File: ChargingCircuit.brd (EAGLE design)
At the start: 100 x 80 mm, 22 parts, among them U1 MAX745EACSSOP

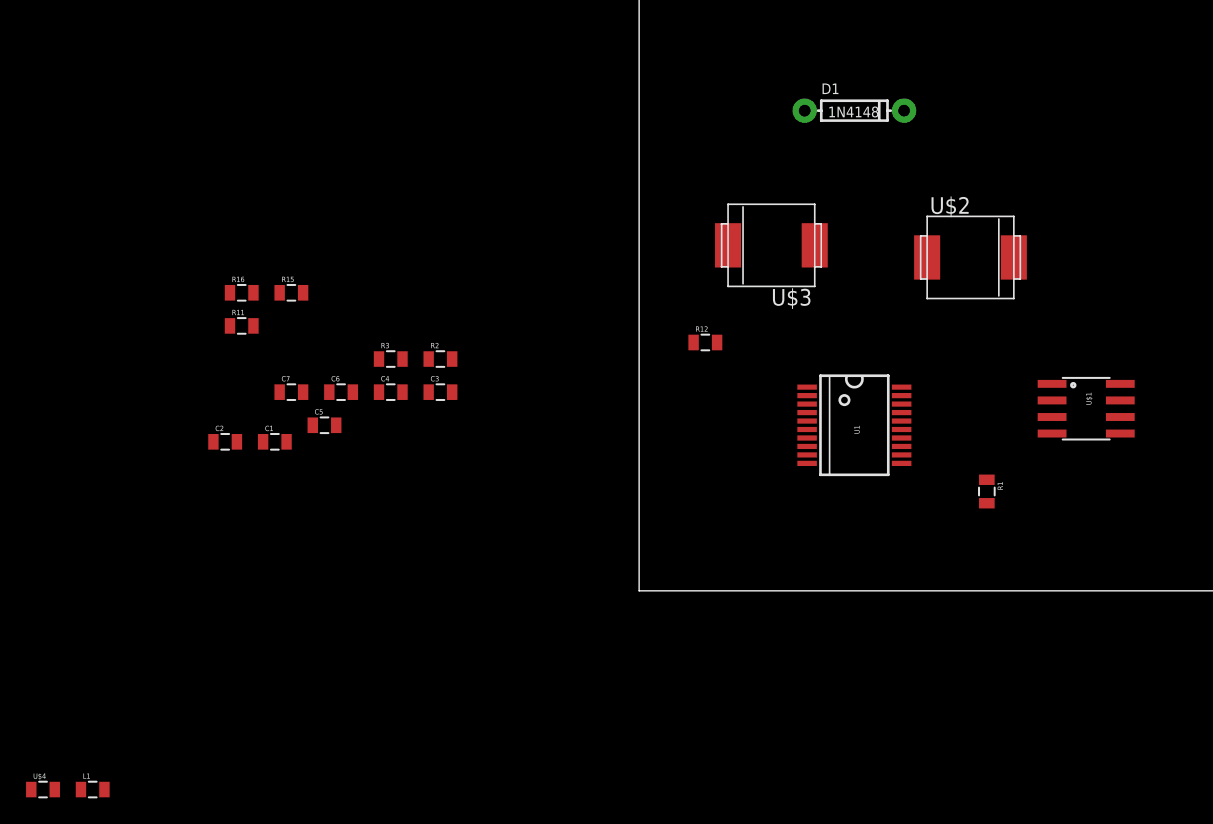
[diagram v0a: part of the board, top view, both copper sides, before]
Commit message: minor changes to charging board
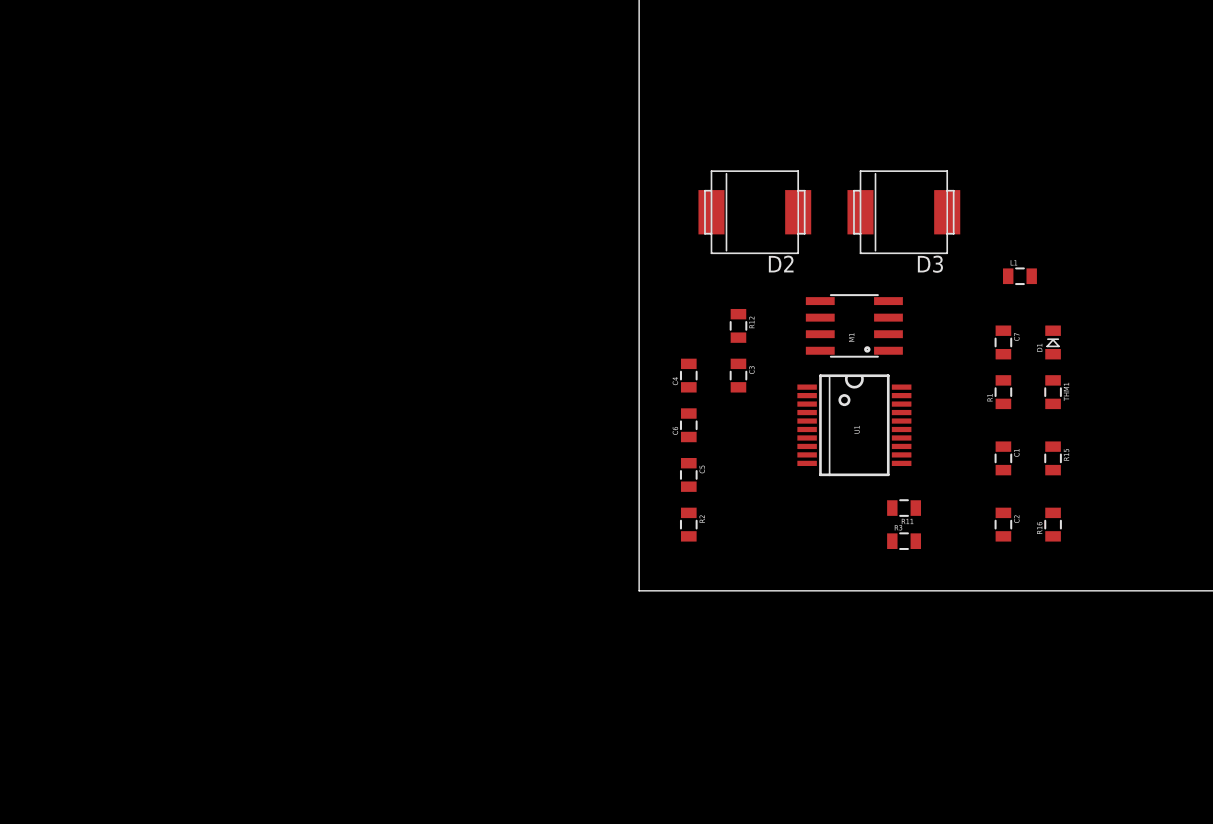
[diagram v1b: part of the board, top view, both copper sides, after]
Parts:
- removed U$1: IRF7303, Work:SO08
- removed U$2, U$3: MBRS340T3, Work:DO-214AB
- removed U$4: THM, Work:0805
- added D2, D3: MBRS340T3, BB8:DO-214AB
- added M1: IRF7303, BB8:SO08
- added THM1: (no value), BB8:0805
- C1: value (none) -> 68uF
- C2, C4, C6, C7: value (none) -> 0.1uF
- C3: value (none) -> 47nF
- D1: value 1N4148 -> 1N4148-0805; device SparkFun-DiscreteSemi:DIODE-1N4148 -> BB8:0805-DIODE
- R11, R3: value (none) -> 100k
- R15, R2: value (none) -> 10k
- moved L1 81.3 mm to (29.2, 24.1)
- moved R16 64.7 mm to (31.8, 5.08), turned to 90 degrees
- moved C2 60.0 mm to (27.9, 5.08), turned to 270 degrees
- moved R15 59.8 mm to (31.8, 10.2), turned to 270 degrees
- moved C1 55.9 mm to (27.9, 10.2), turned to 270 degrees
- moved C7 54.7 mm to (27.9, 19.1), turned to 270 degrees
- moved R11 52.7 mm to (20.3, 6.35), turned to 180 degrees
- moved R3 41.8 mm to (20.3, 3.81)
- moved C5 28.2 mm to (3.81, 8.89), turned to 270 degrees
- moved C6 26.8 mm to (3.81, 12.7), turned to 90 degrees
- moved D1 23.4 mm to (31.8, 19.1), turned to 90 degrees
- moved R2 22.9 mm to (3.81, 5.08), turned to 270 degrees
- moved C3 22.9 mm to (7.62, 16.5), turned to 270 degrees
- moved C4 22.9 mm to (3.81, 16.5), turned to 90 degrees
- moved R1 7.73 mm to (27.9, 15.2), turned to 90 degrees
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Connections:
- net GND: now also D2.POS, M1.3, THM1.1; no longer U$1.3, U$2.POS, U$4.1
- net N$1: now also D1.1; no longer D1.A
- net N$14: now also THM1.2; no longer U$4.2
- net N$2: now also D1.2; no longer D1.C
- net N$3: now also M1.2; no longer U$1.2
- net N$4: now also M1.4; no longer U$1.4
- net N$5: now also D3.NEG; no longer U$3.NEG
- net N$6: now also D3.POS; no longer U$3.POS
- net N$8: now also D2.NEG, M1.1, M1.5, M1.6; no longer U$1.1, U$1.5, U$1.6, U$2.NEG
- net VIN: now also M1.7, M1.8; no longer U$1.7, U$1.8

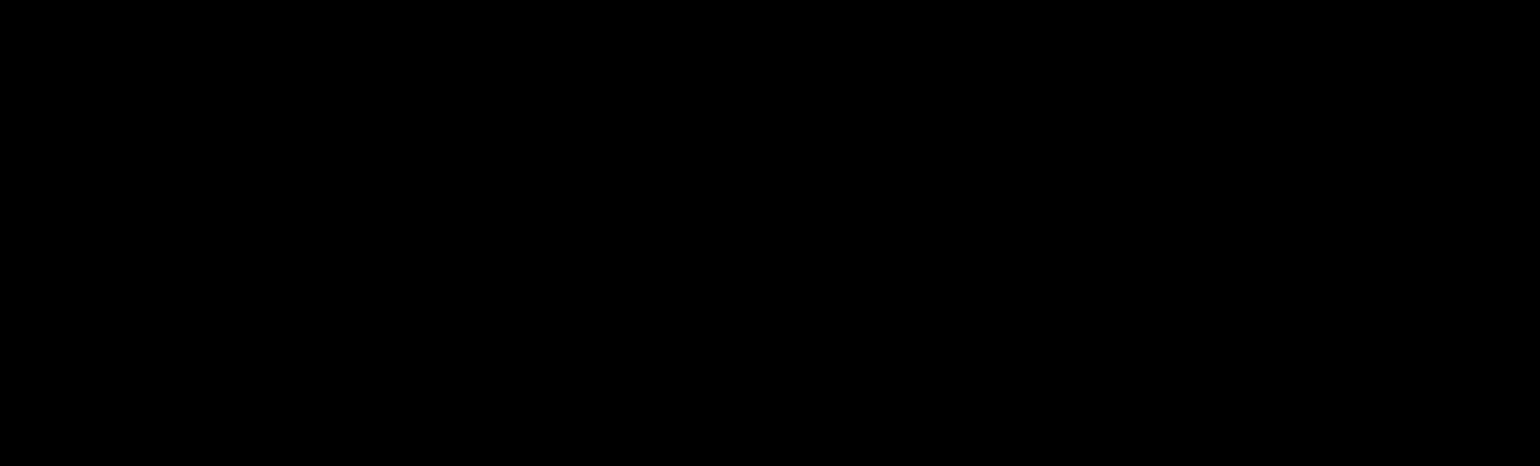
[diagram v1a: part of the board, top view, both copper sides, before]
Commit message: Added wireless charging board, speaker circuit
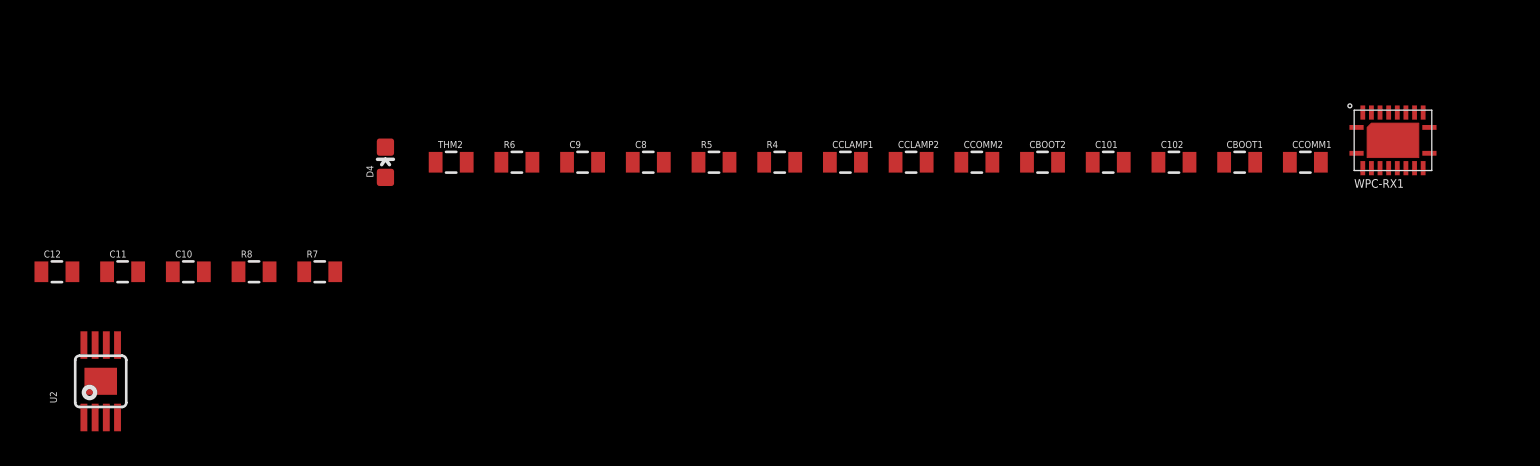
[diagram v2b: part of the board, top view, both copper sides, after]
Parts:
- added C10: 1uF, SparkFun-Capacitors:0805
- added C101, C102, C8, C9, CBOOT1, CBOOT2, CCLAMP1, CCLAMP2, CCOMM1, CCOMM2: (no value), SparkFun-Capacitors:0805
- added C11, C12: 0.1uF, SparkFun-Capacitors:0805
- added D4: BLUE, SparkFun-LED:LED-0603
- added FRAME2, FRAME3: FRAME-LETTERNO_PACKAGE, SparkFun-Aesthetics:DUMMY
- added R4, R5, R6: (no value), SparkFun-Passives:0805
- added R7, R8: 150k, SparkFun-Passives:0805
- added THM2: (no value), BB8:0805
- added U2: TPA2005D1DGN, SparkFun-AnalogIC:POWER-SOP8
- added WPC-RX1: BQ51013B-20VQFN, BB8:20-VQFN
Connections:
- new net AC1: C101.2, C102.1, CBOOT1.1, CCLAMP1.1, CCOMM1.1, WPC-RX1.P$2
- new net AC2: C102.2, CBOOT2.1, CCLAMP2.1, CCOMM2.1
- new net AUDIOIN: C11.1
- new net AUDIO_OUT+: U2.5
- new net AUDIO_OUT-: U2.8
- new net BI-STATE: WPC-RX1.P$10
- new net BI-STATE2: WPC-RX1.P$11
- new net BOOT2: CBOOT2.2
- new net N$16: CCOMM2.2
- new net N$17: CCLAMP2.2
- new net N$18: CCLAMP1.2
- new net N$19: CBOOT1.2
- new net N$20: CCOMM1.2
- new net N$21: C101.1
- new net N$22: R4.1, WPC-RX1.P$12
- new net N$23: R4.2, R5.1, R6.1, WPC-RX1.P$14
- new net N$24: D4.C, WPC-RX1.P$7
- new net N$25: C9.1, R6.2, WPC-RX1.P$18
- new net N$26: R7.2, U2.3
- new net N$28: C11.2, R7.1
- new net N$30: R8.2, U2.4
- new net N$32: C12.1, R8.1
- new net OUT: C8.1, D4.A, WPC-RX1.P$4
- new net SPEAKER_SHUTDOWN: U2.1
- new net TRI-STATE: THM2.1, WPC-RX1.P$13
- new net VDD: U2.6
- new net VDD_5V: C10.1
- net GND: now also C10.2, C12.2, C8.2, C9.2, R5.2, THM2.2, U2.7, U2.9, WPC-RX1.P$1, WPC-RX1.P$20

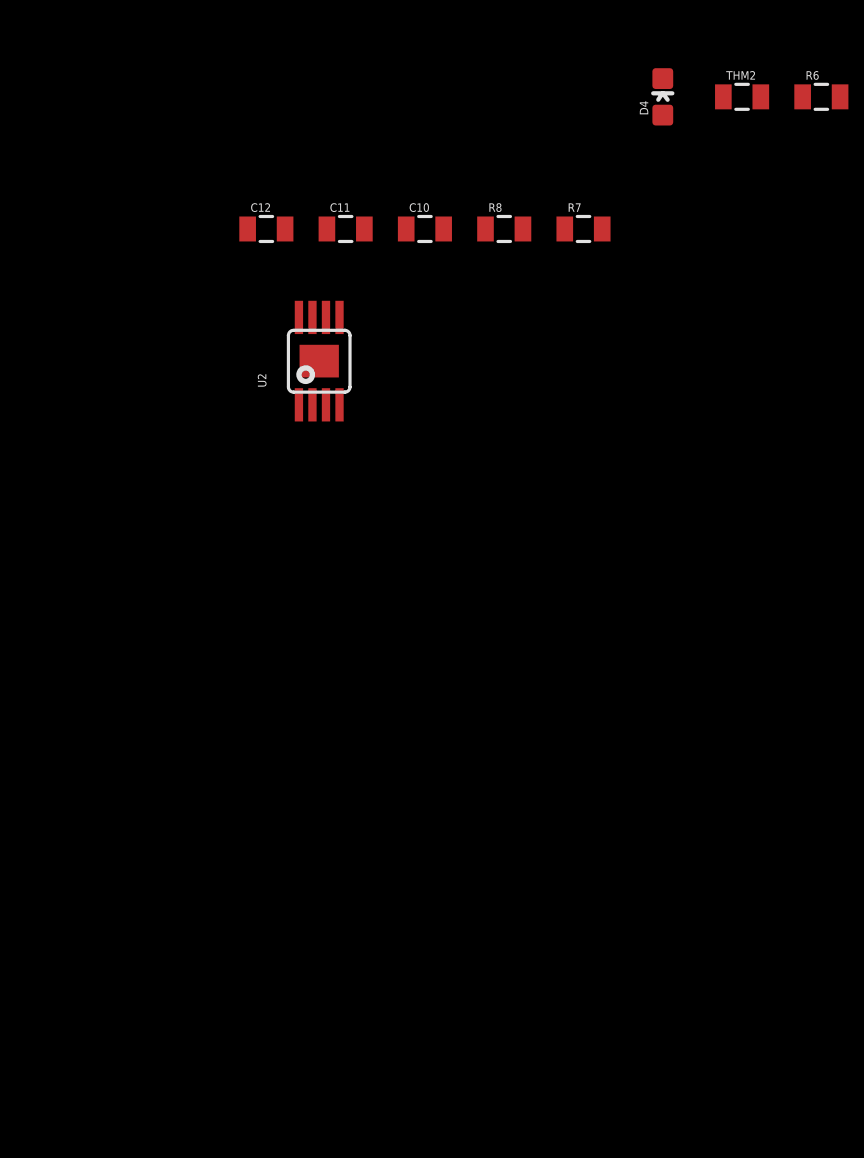
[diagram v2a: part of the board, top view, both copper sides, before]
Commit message: added more info for boards
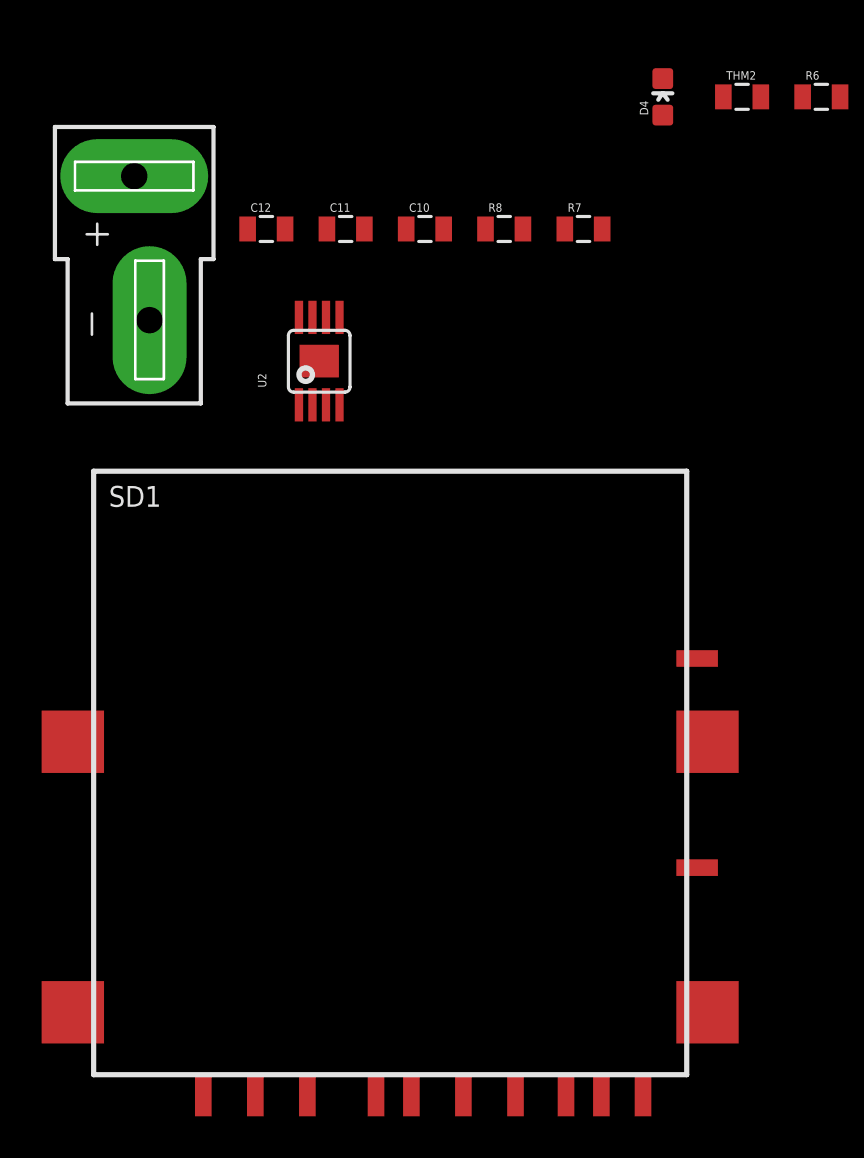
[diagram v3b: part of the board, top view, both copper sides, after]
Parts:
- added FRAME4: FRAME-LETTERNO_PACKAGE, SparkFun-Aesthetics:DUMMY
- added J1: BATTERY_CONNDEANS, SparkFun-Connectors:DEANS
- added SD1: 5738-SDCARD, BB8:SD-5738
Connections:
- new net CS: SD1.P$1
- new net MISO: SD1.P$7
- new net MOSI: SD1.P$2
- new net N$27: SD1.P$4
- new net SCK: SD1.P$5
- net GND: now also J1.-, SD1.P$3, SD1.P$6
- net N$7: now also J1.+
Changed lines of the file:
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@@
 <element name="C12" library="SparkFun-Capacitors" package="0805" value="0.1uF" x="-114.3" y="-5.08"/>
 <element name="U2" library="SparkFun-AnalogIC" package="POWER-SOP8" value="TPA2005D1DGN" x="-111.76" y="-11.43"/>
+<element name="J1" library="SparkFun-Connectors" package="DEANS" value="BATTERY_CONNDEANS" x="-120.65" y="-2.54"/>
+<element name="FRAME4" library="SparkFun-Aesthetics" package="DUMMY" value="FRAME-LETTERNO_PACKAGE" x="-124.46" y="-15.24">
+<attribute name="DESIGNER" value="Nobody" x="-124.46" y="-15.24" size="1.778" layer="27" display="off"/>
+<attribute name="VERSION" value="v01" x="-124.46" y="-15.24" size="1.778" layer="27" display="off"/>
+</element>
+<element name="SD1" library="BB8" package="SD-5738" value="5738-SDCARD" x="-107.95" y="-45.72"/>
 </elements>
 <signals>
@@
 <contactref element="U2" pad="9"/>
 <contactref element="U2" pad="7"/>
+<contactref element="J1" pad="-"/>
+<contactref element="SD1" pad="P$3"/>
+<contactref element="SD1" pad="P$6"/>
+<wire x1="-102.33" y1="-46.72" x2="-109.03" y2="-46.72" width="0" layer="19" extent="1-1"/>
+<wire x1="-111.76" y1="-11.43" x2="-109.03" y2="-46.72" width="0" layer="19" extent="1-1"/>
 <wire x1="-112.085" y1="-9.33" x2="-111.76" y2="-11.43" width="0" layer="19" extent="1-1"/>
 <wire x1="-113.4" y1="-5.08" x2="-112.085" y2="-9.33" width="0" layer="19" extent="1-1"/>
 <wire x1="-105.78" y1="-5.08" x2="-112.085" y2="-9.33" width="0" layer="19" extent="1-1"/>
+<wire x1="-119.9134" y1="-9.4615" x2="-112.085" y2="-9.33" width="0" layer="19" extent="1-1"/>
 <wire x1="-90.54" y1="1.27" x2="-105.78" y2="-5.08" width="0" layer="19" extent="1-1"/>
 <wire x1="-82.92" y1="1.27" x2="-90.54" y2="1.27" width="0" layer="19" extent="1-1"/>
@@
 <contactref element="R1" pad="1"/>
 <contactref element="C1" pad="1"/>
-<wire x1="27.94" y1="11.06" x2="27.94" y2="14.34" width="0" layer="19" extent="1-1"/>
-<wire x1="20.135" y1="11.725" x2="27.94" y2="11.06" width="0" layer="19" extent="1-1"/>
+<contactref element="J1" pad="+"/>
+<wire x1="20.135" y1="11.725" x2="-120.65" y2="-2.54" width="0" layer="19" extent="1-1"/>
+<wire x1="27.94" y1="11.06" x2="20.135" y2="11.725" width="0" layer="19" extent="1-1"/>
+<wire x1="27.94" y1="14.34" x2="27.94" y2="11.06" width="0" layer="19" extent="1-1"/>
 </signal>
 <signal name="STATUS">
@@
 <contactref element="U2" pad="8"/>
 </signal>
+<signal name="SCK">
+<contactref element="SD1" pad="P$5"/>
+</signal>
+<signal name="MISO">
+<contactref element="SD1" pad="P$7"/>
+</signal>
+<signal name="N$27">
+<contactref element="SD1" pad="P$4"/>
+</signal>
+<signal name="CS">
+<contactref element="SD1" pad="P$1"/>
+</signal>
+<signal name="MOSI">
+<contactref element="SD1" pad="P$2"/>
+</signal>
 </signals>

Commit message: Added BQ40Z60 Charging Circuit
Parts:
- removed FRAME1, FRAME2, FRAME3, FRAME4: FRAME-LETTERNO_PACKAGE, SparkFun-Aesthetics:DUMMY
- added C13, C17: 22pF, SparkFun-Capacitors:0805
- added C14, C15, C16, C18, C19, C20, C21, C24, C25, C26, C28, C29, C30, C31, C32, C33, C34, C35, C36, C37, C38, C39, C40: 0.1uF, SparkFun-Capacitors:0805
- added C22, C23, C27: 2.2uF, SparkFun-Capacitors:0805
- added D5, D6: MBRA140, SparkFun-DiscreteSemi:SMA-DIODE
- added D7, D8: 1N4148-0805, BB8:0805-DIODE
- added FRAME6, FRAME7, FRAME8, FRAME9: FRAME-LEDGER, SparkFun-Aesthetics:CREATIVE_COMMONS
- added J2: (no value), SparkFun-Connectors:1X04-1.5MM_JST
- added L2: 2.2uH, SparkFun-Passives:0805
- added Q1, Q2, Q3, Q4, Q5, Q6, Q7: CSD17308Q3, BB8:SON-8
- added R10, R40, R46, R47: 1k, SparkFun-Resistors:0805
- added R13, R14, R17, R18, R19, R37, R38, R39, R41, R42, R45, R9: 100, SparkFun-Resistors:0805
- added R20: 35.63k, SparkFun-Resistors:0805
- added R21: 332k, SparkFun-Resistors:0805
- added R22: 10m, SparkFun-Resistors:0805
- added R23, R32: 10k, SparkFun-Resistors:0805
- added R24, R25, R30, R33, R35, R44: 5.1k, SparkFun-Resistors:0805
- added R26: 1, SparkFun-Resistors:0805
- added R27: 100k, SparkFun-Resistors:0805
- added R28: 2, SparkFun-Resistors:0805
- added R29, R31, R34: 10M, SparkFun-Resistors:0805
- added R36: 10, SparkFun-Resistors:0805
- added R43: 5m, SparkFun-Resistors:0805
- added RT1: 10k-PTC, BB8:0805
- added RT2, RT3, RT4: (no value), BB8:0805
- added U3: BQ40Z60, BB8:S-PVQFN-N32
- added U4: BQ2947, BB8:WSON-8
- added Z1, Z2, Z3: MM3Z75VC, BB8:SOD-323F
- THM1: value (none) -> 10K - NTC
- THM2: value (none) -> 10K-NTC
- moved SD1 202.9 mm to (82.5, 24.1), turned to 180 degrees
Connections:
- removed net VDD: U2.6
- new net ALERT: R9.2
- new net N$29: R10.1, R13.2, Z1.2
- new net N$31: RT1.1, U3.P$10
- new net N$33: RT2.1, U3.P$11
- new net N$34: RT3.1, U3.P$12
- new net N$35: RT4.1, U3.P$13
- new net N$36: R9.1, U3.P$14
- new net N$37: Q1.P$5, Q1.P$6, Q1.P$7, Q1.P$8, Q3.P$4, R24.1, R29.2
- new net N$38: R13.1, U3.P$15
- new net N$39: R14.1, U3.P$16
- new net N$40: R14.2, R17.1, Z2.2
- new net N$41: C13.1, R20.2, R21.1, U3.P$18
- new net N$42: R24.2, U3.P$29
- new net N$43: C18.1, C19.2
- new net N$44: R18.1, U3.P$17
- new net N$45: R18.2, R19.1, Z3.2
- new net N$46: C15.1, C16.2, L2.2, Q6.P$1, Q6.P$2, Q6.P$3, R22.2, U3.P$20
- new net N$47: R26.1, U3.P$22
- new net N$48: D6.A, Q1.P$4, R23.1
- new net N$50: C20.2, L2.1, Q2.P$5, Q2.P$6, Q2.P$7, Q2.P$8, U3.P$26
- new net N$51: C20.1, D5.C, U3.P$28
- new net N$52: C21.1, D5.A, U3.P$23
- new net N$53: C23.2, Q3.P$5, Q3.P$6, Q3.P$7, Q3.P$8, Q6.P$5, Q6.P$6, Q6.P$7, Q6.P$8, R26.2
- new net N$54: R25.1, U3.P$21
- new net N$55: C26.1, Q7.P$4, R25.2, R35.1, R44.2
- new net N$56: Q6.P$4, U3.P$27
- new net N$57: D6.C, D7.2
- new net N$58: C22.2, R28.2
- new net N$59: Q2.P$4, U3.P$25
- new net N$60: R30.2, U3.P$31
- new net N$61: Q4.P$4, R30.1, R31.2
- new net N$62: R32.2, U3.P$30
- new net N$63: Q4.P$5, Q4.P$6, Q4.P$7, Q4.P$8, Q5.P$5, Q5.P$6, Q5.P$7, Q5.P$8
- new net N$64: C24.2, C25.1
- new net N$65: C24.1, Q5.P$1, Q5.P$2, Q5.P$3, R34.1
- new net N$66: Q5.P$4, R33.1, R34.2
- new net N$67: R33.2, U3.P$32
- new net N$68: C40.1, U4.P$7
- new net N$69: J2.1, R36.1, R37.1, R40.2, R45.2
- new net N$70: D8.2, U3.P$1
- new net N$71: D8.1, R36.2
- new net N$72: C27.1, U3.P$2
- new net N$73: C28.1, R37.2, U3.P$3
- new net N$74: C28.2, C29.1, R38.2, U3.P$4
- new net N$75: C29.2, C30.1, R39.2, U3.P$5
- new net N$76: C31.1, U3.P$6
- new net N$77: C32.1, C33.1, R41.2, U3.P$7
- new net N$78: C33.2, C34.1, R42.2, U3.P$8
- new net N$79: R44.1, U4.P$8
- new net N$80: C36.1, R40.1, U4.P$2
- new net N$81: J2.2, R38.1, R46.2
- new net N$82: J2.3, R39.1, R47.1
- new net N$83: C35.1, R45.1, U4.P$1
- new net N$84: C36.2, C37.1, R46.1, U4.P$3
- new net N$85: C37.2, C39.2, R47.2, U4.P$4
- new net N$86: C38.1, U4.P$5
- new net PACK+: C18.2, D7.1, Q1.P$1, Q1.P$2, Q1.P$3, Q3.P$1, Q3.P$2, Q3.P$3, R27.1, R28.1, R29.1, R32.1
- new net PACK-: R41.1, R43.2
- new net SMBC: R19.2
- new net SMBD: R17.2
- new net SYSPRES: R10.2
- new net SYSTEMLOAD: C13.2, C14.1, C16.1, C17.2, C25.2, Q4.P$1, Q4.P$2, Q4.P$3, R21.2, R22.1, R31.1, U3.P$19
- net AC2: now also WPC-RX1.P$19
- net BOOT2: now also WPC-RX1.P$17
- net GND: now also C14.2, C15.2, C17.1, C19.1, C21.2, C22.1, C23.1, C26.2, C27.2, C30.2, C31.2, C32.2, C34.2, C35.2, C38.2, C39.1, C40.2, J2.4, Q2.P$1, Q2.P$2, Q2.P$3, Q7.P$1, Q7.P$2, Q7.P$3, R20.1, R23.2, R27.2, R35.2, R42.1, R43.1, RT1.2, RT2.2, RT3.2, RT4.2, U3.P$24, U3.P$9, U3.P$GND, U4.P$6, U4.P$GND, WPC-RX1.P$9, Z1.1, Z2.1, Z3.1
- net N$16: now also WPC-RX1.P$15
- net N$17: now also WPC-RX1.P$16
- net N$18: now also WPC-RX1.P$5
- net N$19: now also WPC-RX1.P$3
- net N$20: now also WPC-RX1.P$6
- net VDD_5V: now also U2.6
